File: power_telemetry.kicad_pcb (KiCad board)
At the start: 2 copper layers, 86.5 x 61.5 mm, 50 parts, among them J1 CONN_01X02, J10 CONN_01X04, J11 CONN_01X04, J12 GS2, J13 CONN_01X02, J2 Screw_Terminal_1x02, J3 Screw_Terminal_1x02, J4 CONN_01X03, J5 CONN_01X02, J6 CONN_01X03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

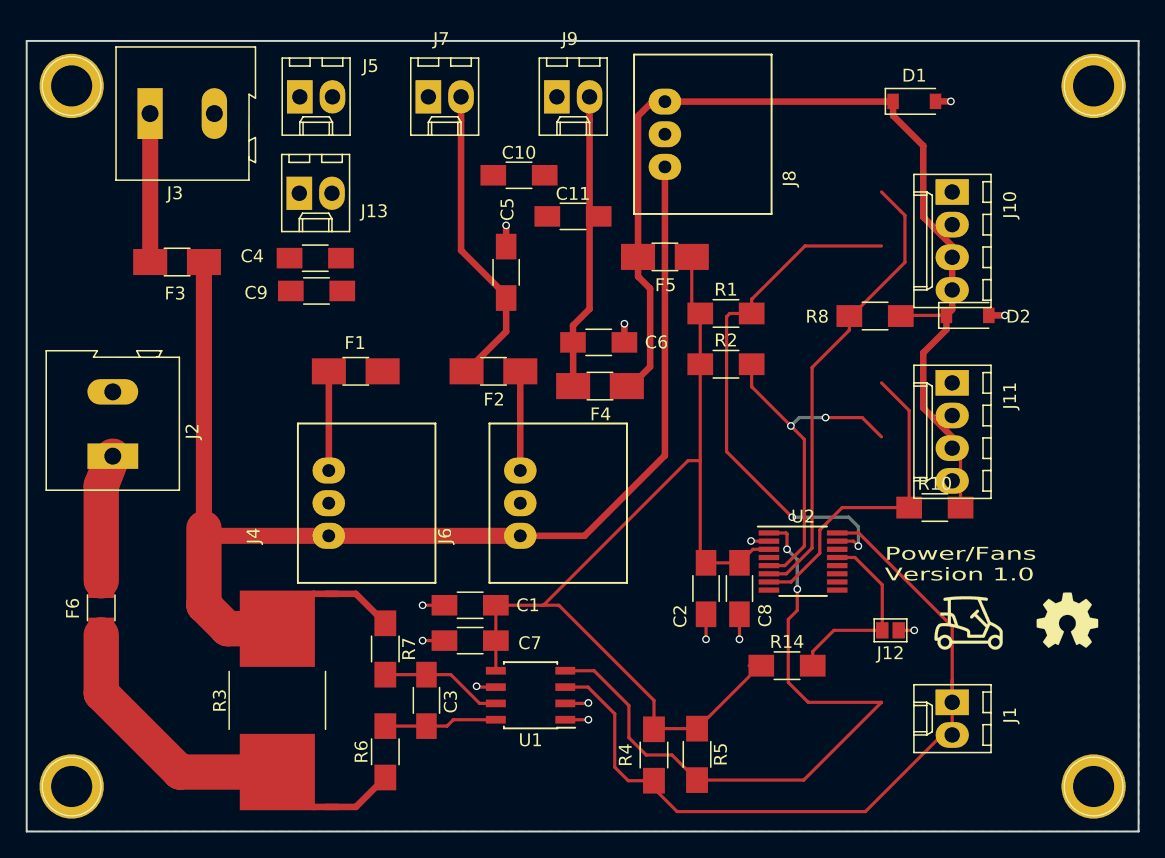
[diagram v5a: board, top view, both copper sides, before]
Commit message: re-annoted all items and starting routing from scratch again
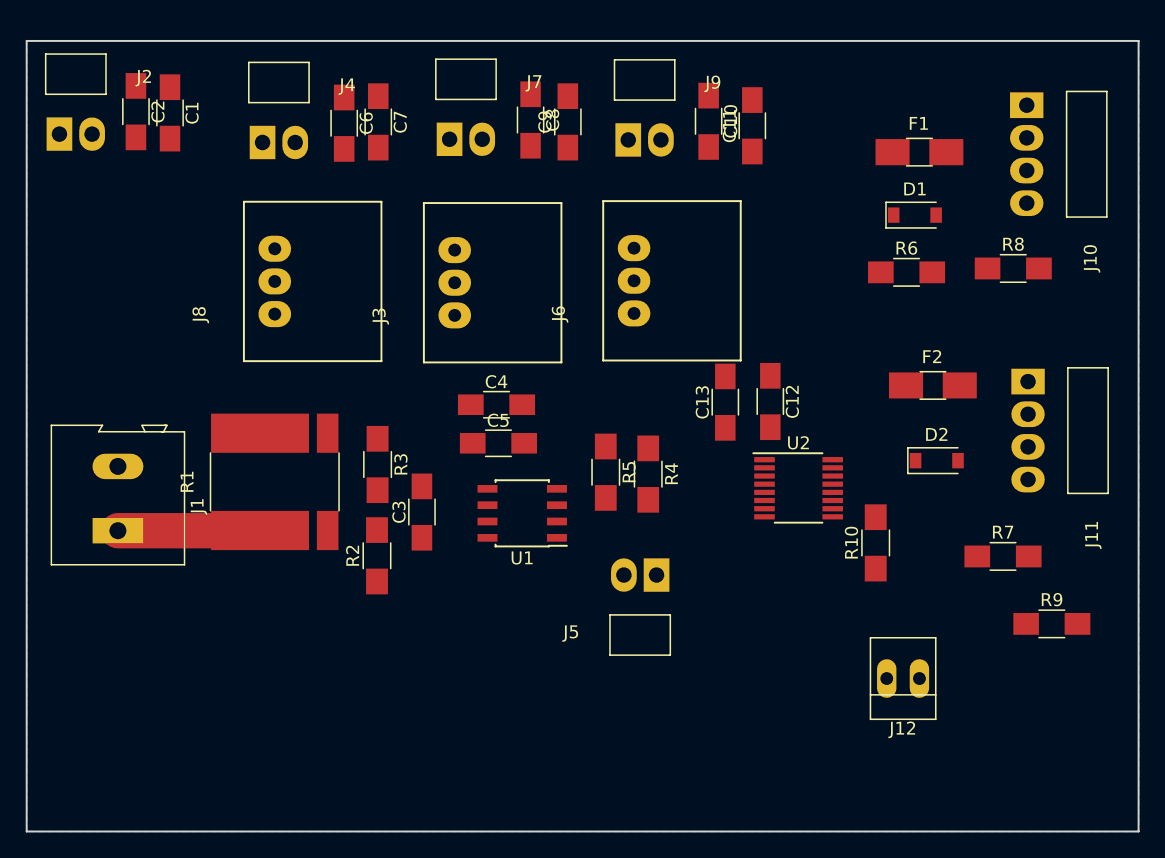
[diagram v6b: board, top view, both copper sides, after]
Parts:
- removed F3: 2.0A PTC, Fuse_Holders_and_Fuses:Fuse_SMD1206_HandSoldering
- removed F4: 1.0A PTC, Fuse_Holders_and_Fuses:Fuse_SMD1206_HandSoldering
- removed F5: 0.5A Polyfuse (confirm size), Fuse_Holders_and_Fuses:Fuse_SMD1206_HandSoldering
- removed F6: 8A Polyfuse, Fuse_Holders_and_Fuses:Fuse_SMD1206_HandSoldering
- removed G***: LOGO, lib_fp:golf_cart
- removed G***: LOGO, lib_fp:OSHW-Logo_2
- removed J13: CONN_01X02, Connectors_Molex:Molex_KK-6410-02_02x2.54mm_Straight
- removed R14: 10k, Resistors_SMD:R_1206_HandSoldering
- removed REF** (x4): 1pin, Connectors:1pin
- added C12: 0.1uF, Capacitors_SMD:C_1206_HandSoldering, F.Cu at (135.3, 77.5)
- added C13: 10uF, Capacitors_SMD:C_1206_HandSoldering, F.Cu at (131.8, 77.6)
- added R9: 10k, Resistors_SMD:R_1206_HandSoldering, F.Cu at (157.2, 94.8)
- C11, C9: value 10uF -> 0.1uF
- C4, C6: value 0.1uF -> 10uF
- F1, F2: value 1.0A PTC -> 0.5A PTC
- J1: value CONN_01X02 -> Screw_Terminal_1x02; footprint Connectors_Molex:Molex_KK-6410-02_02x2.54mm_Straight -> lib_fp:TER-202
- J10, J11: footprint Connectors_Molex:Molex_KK-6410-04_04x2.54mm_Straight -> lib_fp:Molex_KK-171857-04x2.54mm_Right
- J12: footprint Connectors:GS2 -> Connectors:PINHEAD1-2
- J2: value Screw_Terminal_1x02 -> CONN_01X02; footprint lib_fp:TER-202 -> lib_fp:Molex_KK-171857-02x2.54mm_Right
- J3: value Screw_Terminal_1x02 -> CONN_01X03; footprint lib_fp:TER-202 -> lib_fp:DCDC-Conv_Murata_OKI-78SR-E
- J4: value CONN_01X03 -> CONN_01X02; footprint power_telemetry:DCDC-Conv_Murata_OKI-78SR-E -> lib_fp:Molex_KK-171857-02x2.54mm_Right
- J5, J7, J9: footprint Connectors_Molex:Molex_KK-6410-02_02x2.54mm_Straight -> lib_fp:Molex_KK-171857-02x2.54mm_Right
- J6, J8: footprint power_telemetry:DCDC-Conv_Murata_OKI-78SR-E -> lib_fp:DCDC-Conv_Murata_OKI-78SR-E
- R1: value 10k -> .05k; footprint Resistors_SMD:R_1206_HandSoldering -> lib_fp:R_3637_HandSoldering
- R2: value 10k -> 0k
- R3: value .04k -> 0k; footprint power_telemetry:R_4527_HandSoldering -> Resistors_SMD:R_1206_HandSoldering
- R6, R7: value 0k -> 10k
- moved J1 66.3 mm to (84.6, 87.6), turned to 90 degrees
- moved C2 57.8 mm to (86.0, 55.0)
- moved R6 55.1 mm to (145.9, 67.5), turned to 0 degrees
- moved R7 48.6 mm to (153.4, 89.6), turned to 0 degrees
- moved F1 47.0 mm to (146.9, 58.1)
- moved J5 46.4 mm to (126.5, 91.0), turned to 180 degrees
- moved C1 44.9 mm to (88.7, 55.1), turned to 270 degrees
- moved C7 41.0 mm to (104.8, 55.8), turned to 270 degrees
- moved C8 39.9 mm to (116.7, 55.6)
- moved R1 37.5 mm to (96.8, 83.8), turned to 90 degrees
- moved F2 34.2 mm to (148.0, 76.3), turned to 0 degrees
- moved J8 32.4 mm to (96.8, 70.8)
- moved J4 31.0 mm to (95.8, 57.4), turned to 0 degrees
- moved R2 31.0 mm to (104.8, 89.5), turned to 90 degrees
- moved J3 28.4 mm to (110.8, 70.8), turned to 90 degrees
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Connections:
- C1 pad 1: VCC -> GND
- C1 pad 2: GND -> +12V
- C10 pad 2: Net-(C10-Pad2) -> VCC
- C11 pad 1: GND -> VCC
- C11 pad 2: Net-(C11-Pad2) -> GND
- C2 pad 1: VCC -> GND
- C2 pad 2: GND -> +12V
- C4 pad 1: GND -> VCC
- C4 pad 2: Net-(C4-Pad2) -> GND
- C5 pad 1: Net-(C10-Pad2) -> VCC
- C6 pad 1: Net-(C11-Pad2) -> GND
- C6 pad 2: GND -> VCC
- C7 pad 1: VCC -> GND
- C7 pad 2: GND -> VCC
- C8 pad 1: VCC -> GND
- C8 pad 2: GND -> VCC
- C9 pad 1: GND -> VCC
- C9 pad 2: Net-(C4-Pad2) -> GND
- F1 pad 2: Net-(C4-Pad2) -> Net-(F1-Pad2)
- F2 pad 2: Net-(C10-Pad2) -> Net-(F2-Pad2)
- J1 pad 1: /SDA -> Net-(J1-Pad1)
- J1 pad 2: /SCL -> GND
- J10 pad 2: VCC -> Net-(F1-Pad2)
- J11 pad 2: VCC -> Net-(F2-Pad2)
- J2 pad 1: Net-(F6-Pad2) -> GND
- J2 pad 2: GND -> +12V
- J3 pad 1: Net-(F3-Pad2) -> +12V
- J4 pad 1: +12V -> GND
- J4 pad 2: GND -> VCC
- J5 pad 1: GND -> /SDA
- J5 pad 2: Net-(C4-Pad2) -> /SCL
- J7 pad 2: Net-(C10-Pad2) -> VCC
- J9 pad 2: Net-(C11-Pad2) -> VCC
- R1 pad 1: VCC -> Net-(J1-Pad1)
- R1 pad 2: Net-(J10-Pad4) -> +12V
- R10 pad 1: Net-(J11-Pad3) -> VCC
- R10 pad 2: VCC -> Net-(J12-Pad2)
- R2 pad 1: VCC -> Net-(J1-Pad1)
- R2 pad 2: Net-(J11-Pad4) -> Net-(C3-Pad1)
- R3 pad 1: Net-(F6-Pad1) -> +12V
- R3 pad 2: +12V -> Net-(C3-Pad2)
- R6 pad 1: Net-(F6-Pad1) -> VCC
- R6 pad 2: Net-(C3-Pad1) -> Net-(J10-Pad4)
- R7 pad 1: +12V -> VCC
- R7 pad 2: Net-(C3-Pad2) -> Net-(J11-Pad4)
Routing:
- net VCC: track 168.7 -> 0.00 mm
- net +12V: track 106.0 -> 0.00 mm
- net /SCL: track 63.1 -> 0.00 mm, vias 2 -> 0
- net /SDA: track 51.5 -> 0.00 mm
- net Net-(J10-Pad4): track 41.5 -> 0.00 mm, vias 2 -> 0
- net Net-(J10-Pad3): track 37.8 -> 0.00 mm
- net Net-(J11-Pad3): track 32.8 -> 0.00 mm
- net Net-(F6-Pad1): track 31.3 -> 0.00 mm
- net Net-(J11-Pad4): track 27.9 -> 0.00 mm, vias 2 -> 0
- net Net-(C10-Pad2): track 24.1 -> 0.00 mm
- net Net-(C11-Pad2): track 23.0 -> 0.00 mm
- net GND: track 21.0 -> 0.00 mm, vias 13 -> 0
- net Net-(J12-Pad2): track 15.3 -> 0.00 mm
- net Net-(F3-Pad2): track 11.6 -> 0.00 mm
- net Net-(J1-Pad1): track 0.00 -> 11.1 mm
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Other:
- board text removed: "Power/Fans Version 1.0"

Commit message: progress on pcb layout
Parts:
- removed D1, D2: D, Diodes_SMD:D_SOD-123
- added C14: 0.1uF, Capacitors_SMD:C_1206_HandSoldering, F.Cu at (150.3, 73.0)
- added C15: 10uF, Capacitors_SMD:C_1206_HandSoldering, F.Cu at (149.4, 59.2)
- added C16: 10uF, Capacitors_SMD:C_1206_HandSoldering, F.Cu at (146.8, 72.8)
- added C17: 0.1uF, Capacitors_SMD:C_1206_HandSoldering, F.Cu at (152.0, 59.2)
- added REF**: MountingHole_2.5mm, Mounting_Holes:MountingHole_2.5mm, F.Cu at (160.5, 107.5)
- added REF**: MountingHole_2.5mm, Mounting_Holes:MountingHole_2.5mm, F.Cu at (81.0, 107.5)
- added REF**: MountingHole_2.5mm, Mounting_Holes:MountingHole_2.5mm, F.Cu at (160.5, 53.0)
- added REF**: MountingHole_2.5mm, Mounting_Holes:MountingHole_2.5mm, F.Cu at (81.0, 53.0)
- moved J5 29.9 mm to (156.1, 86.8), turned to 270 degrees
- moved R9 17.6 mm to (149.0, 79.2), turned to 180 degrees
- moved J2 16.0 mm to (85.0, 72.0), turned to 90 degrees
- moved C2 11.4 mm to (83.0, 66.0), turned to 0 degrees
- moved C7 10.9 mm to (94.0, 55.0)
- moved J12 10.1 mm to (146.0, 89.0)
- moved C1 10.0 mm to (83.0, 63.4), turned to 0 degrees
- moved C12 9.79 mm to (127.9, 83.9), turned to 180 degrees
- moved C9 9.63 mm to (110.0, 55.0)
- moved F2 9.28 mm to (140.0, 71.6), turned to 270 degrees
- moved R7 8.46 mm to (149.1, 82.3)
- moved F1 7.90 mm to (140.0, 61.9), turned to 90 degrees
- moved J4 7.86 mm to (88.0, 57.0)
- moved R8 7.30 mm to (147.6, 64.2), turned to 180 degrees
- moved J7 6.40 mm to (104.0, 57.0)
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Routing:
- net +12V: track 0.00 -> 68.9 mm
- net VCC: track 0.00 -> 49.0 mm
- net Net-(C3-Pad2): track 0.00 -> 6.93 mm
- net Net-(C3-Pad1): track 0.00 -> 6.74 mm
- net Net-(J1-Pad1): track 11.1 -> 16.2 mm
- removed copper zone on B.Cu, net GND

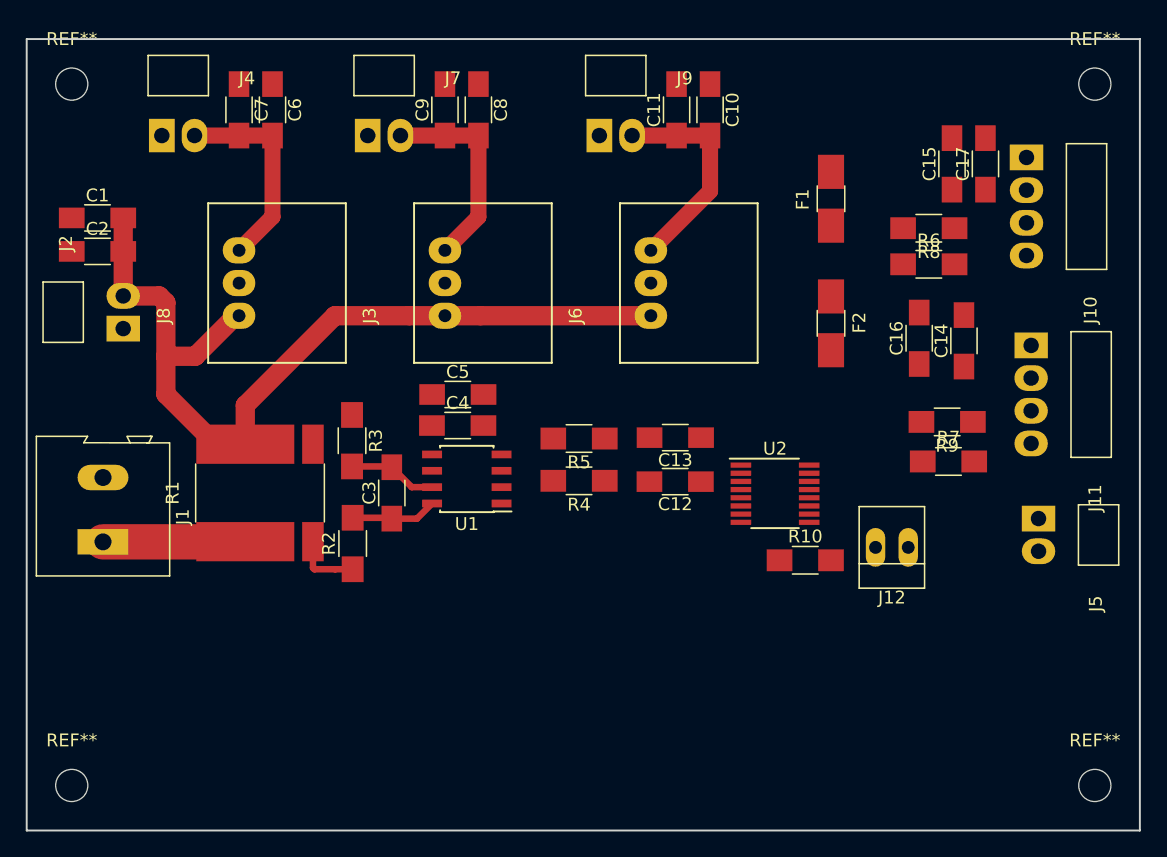
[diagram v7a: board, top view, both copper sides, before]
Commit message: pcb now has all connections made
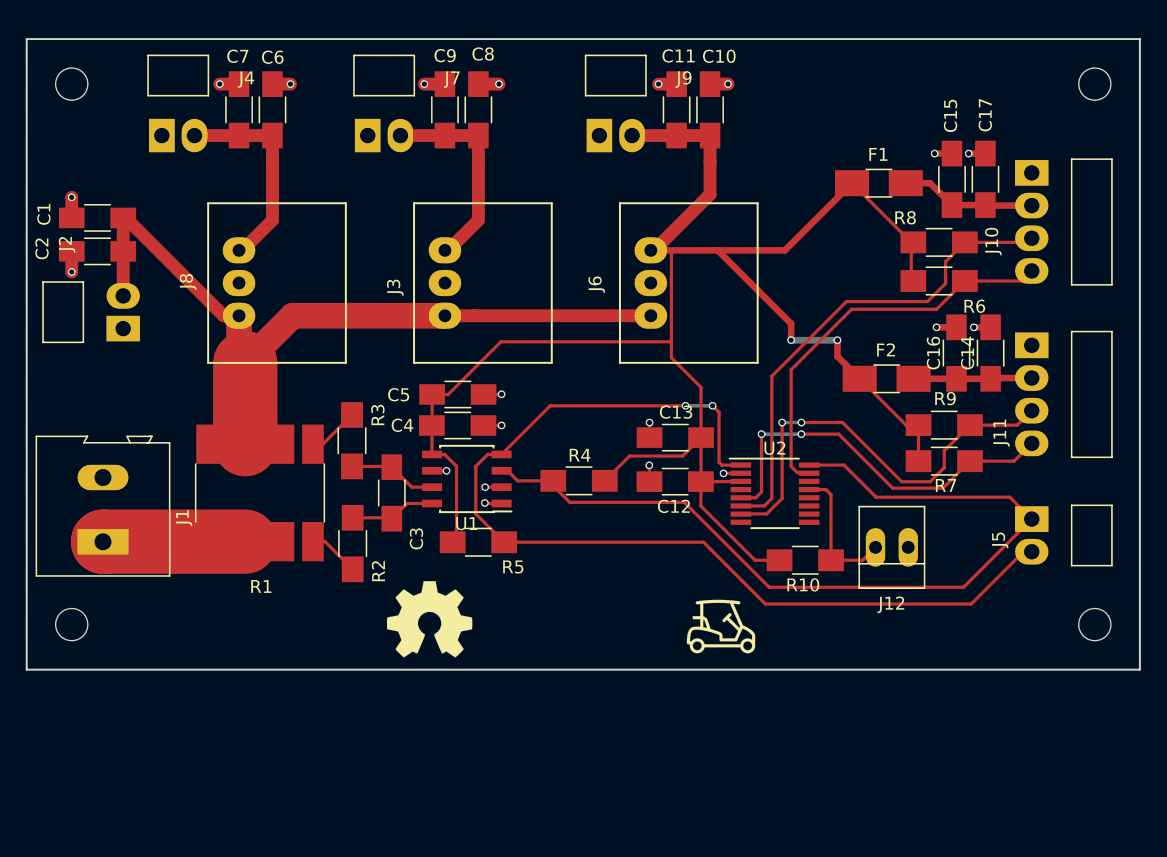
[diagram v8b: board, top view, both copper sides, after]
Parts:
- added G***: LOGO, lib_fp:golf_cart, F.Cu at (131.5, 95.2)
- added REF***: OSHW-Symbol_6.7x6mm_SilkScreen, Symbols:OSHW-Symbol_6.7x6mm_SilkScreen, F.Cu at (108.8, 94.6)
- moved REF** 12.5 mm to (160.5, 95.0)
- moved REF** 12.5 mm to (81.0, 95.0)
- moved R5 11.2 mm to (112.6, 88.6), turned to 0 degrees
- moved F2 6.11 mm to (144.3, 75.9), turned to 0 degrees
- moved F1 3.92 mm to (143.7, 60.7), turned to 0 degrees
- moved C16 3.12 mm to (149.8, 73.9)
- moved C14 2.28 mm to (152.4, 73.9)
- moved R6 1.53 mm to (148.4, 68.3)
- moved R8 1.36 mm to (148.4, 65.3)
- moved J10 1.27 mm to (155.6, 59.9)
- moved C15 1.20 mm to (149.4, 60.4)
- moved C17 1.20 mm to (152.0, 60.4)
- moved J5 0.53 mm to (155.6, 86.8)
- moved R9 0.34 mm to (148.8, 79.5)
- moved R7 0.33 mm to (148.8, 82.3)
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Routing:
- net VCC: track 49.0 -> 178.3 mm, vias 0 -> 2
- net /SCL: track 0.00 -> 78.2 mm, vias 0 -> 2
- net /SDA: track 0.00 -> 66.4 mm
- net Net-(J10-Pad3): track 0.00 -> 37.8 mm
- net Net-(J11-Pad3): track 0.00 -> 34.0 mm, vias 0 -> 2
- net Net-(J10-Pad4): track 0.00 -> 31.0 mm
- net Net-(J11-Pad4): track 0.30 -> 30.5 mm, vias 0 -> 2
- net GND: track 0.00 -> 27.9 mm, vias 0 -> 20
- net Net-(J12-Pad2): track 0.00 -> 10.8 mm
- net Net-(C15-Pad1): track 0.00 -> 10.5 mm
- net Net-(C14-Pad1): track 0.00 -> 9.21 mm
- net +12V: track 68.9 -> 65.5 mm
- net Net-(J1-Pad1): track 16.2 -> 15.0 mm
- added copper zone on B.Cu, net GND
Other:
- board size 86.5 x 61.5 mm -> 86.5 x 49 mm
